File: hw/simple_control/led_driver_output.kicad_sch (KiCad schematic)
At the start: 9 parts

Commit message: [hw] Complete root schematics of simple control
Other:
- company: (none) -> Stefan Misik
- title: (none) -> WS2812 Simple Controller
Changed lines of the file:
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@@
 (kicad_sch (version 20230121) (generator eeschema)
   (paper "A4")
+  (title_block
+    (title "WS2812 Simple Controller")
+    (date "2023-03-09")
+    (company "Stefan Misik")
+    (comment 1 "LED Driver Output Stage")
+  )
   (junction (at 107.95 118.11) (diameter 0) (color 0 0 0 0)
   )

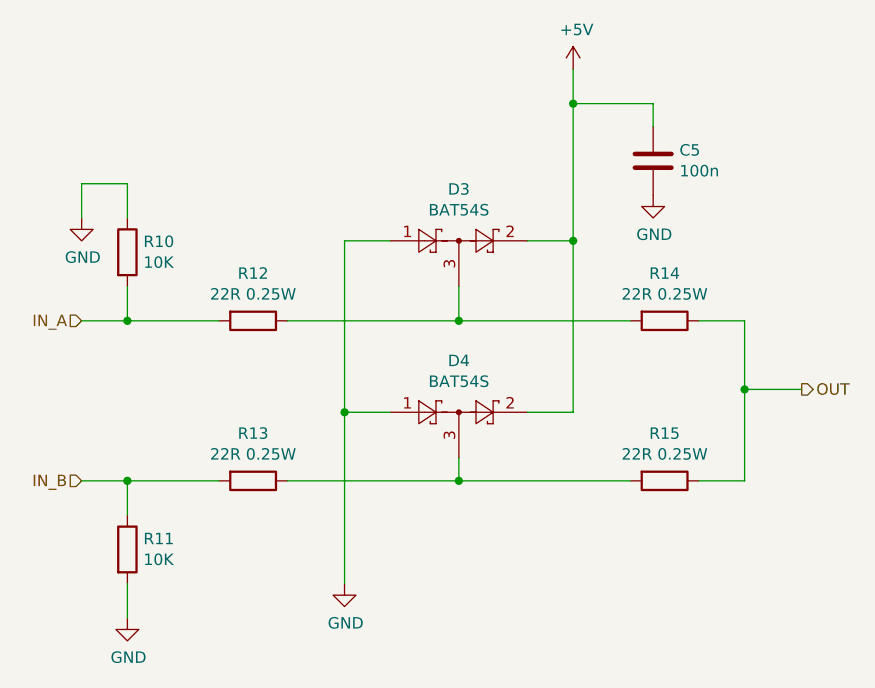
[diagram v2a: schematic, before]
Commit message: [hw] Add CPU modules
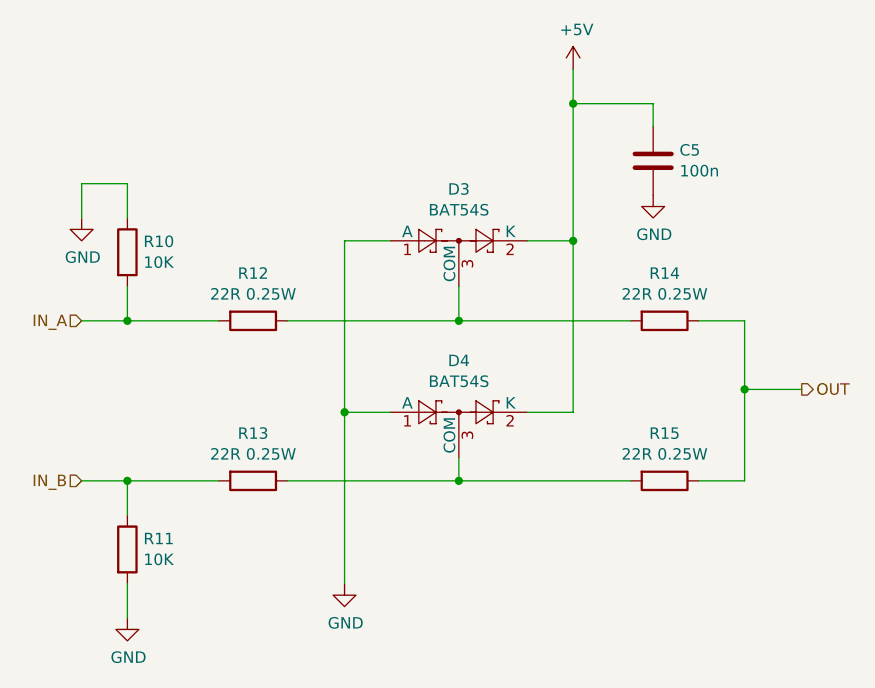
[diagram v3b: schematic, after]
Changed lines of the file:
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@@
     )
   )
-  (symbol (lib_name "GND_3") (lib_id "power:GND") (at 132.08 129.54 0) (unit 1)
+  (symbol (lib_id "power:GND") (at 132.08 129.54 0) (unit 1)
     (in_bom yes) (on_board yes) (dnp no)
     (property "Reference" "#PWR09" (at 132.08 135.89 0)
@@
     )
   )
-  (symbol (lib_name "GND_2") (lib_id "power:GND") (at 166.37 86.36 0) (unit 1)
+  (symbol (lib_id "power:GND") (at 166.37 86.36 0) (unit 1)
     (in_bom yes) (on_board yes) (dnp no)
     (property "Reference" "#PWR011" (at 166.37 92.71 0)
@@
     )
   )
-  (symbol (lib_name "GND_1") (lib_id "power:GND") (at 102.87 88.9 0) (unit 1)
+  (symbol (lib_id "power:GND") (at 102.87 88.9 0) (unit 1)
     (in_bom yes) (on_board yes) (dnp no)
     (property "Reference" "#PWR07" (at 102.87 95.25 0)
@@
     )
   )
-  (symbol (lib_name "BAT54S_1") (lib_id "Diode:BAT54S") (at 144.78 110.49 0) (unit 1)
+  (symbol (lib_id "Diode:BAT54S") (at 144.78 110.49 0) (unit 1)
     (in_bom yes) (on_board yes) (dnp no)
     (property "Reference" "D4" (at 144.78 104.775 0)

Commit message: [hw] Wire some RPi Pico/Zero connections
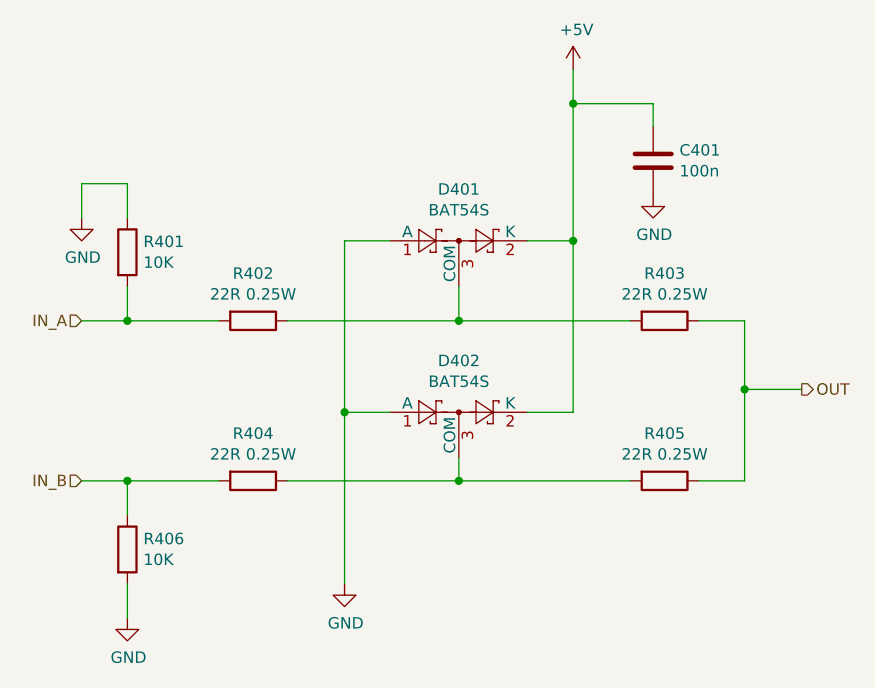
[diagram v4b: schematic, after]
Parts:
- renumbered C5 to C401, D3 to D401, D4 to D402, R10 to R401, R12 to R402, R14 to R403, R13 to R404, R15 to R405, R11 to R406
